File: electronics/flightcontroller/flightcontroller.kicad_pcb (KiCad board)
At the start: 2 copper layers, 30 x 50 mm, 81 parts, among them J1 BAT+, J10 USB, J11 Payload, J12 BAT-, J13 Conn_01x04, J2 ESC+, J3 ESC, J4 Servo3, J5 Servo2, J6 Servo1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

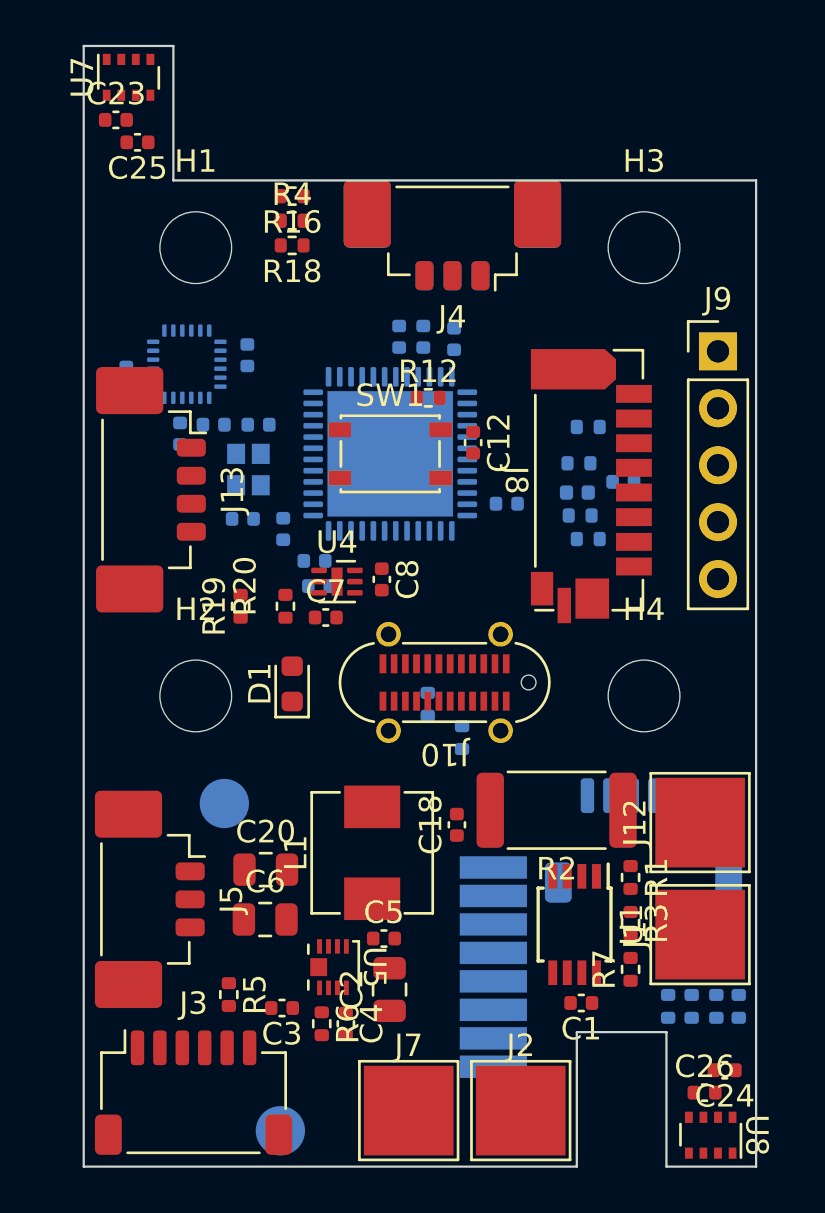
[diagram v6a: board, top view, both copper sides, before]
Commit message: electronics: Finished wiring of the flight controller PCB.
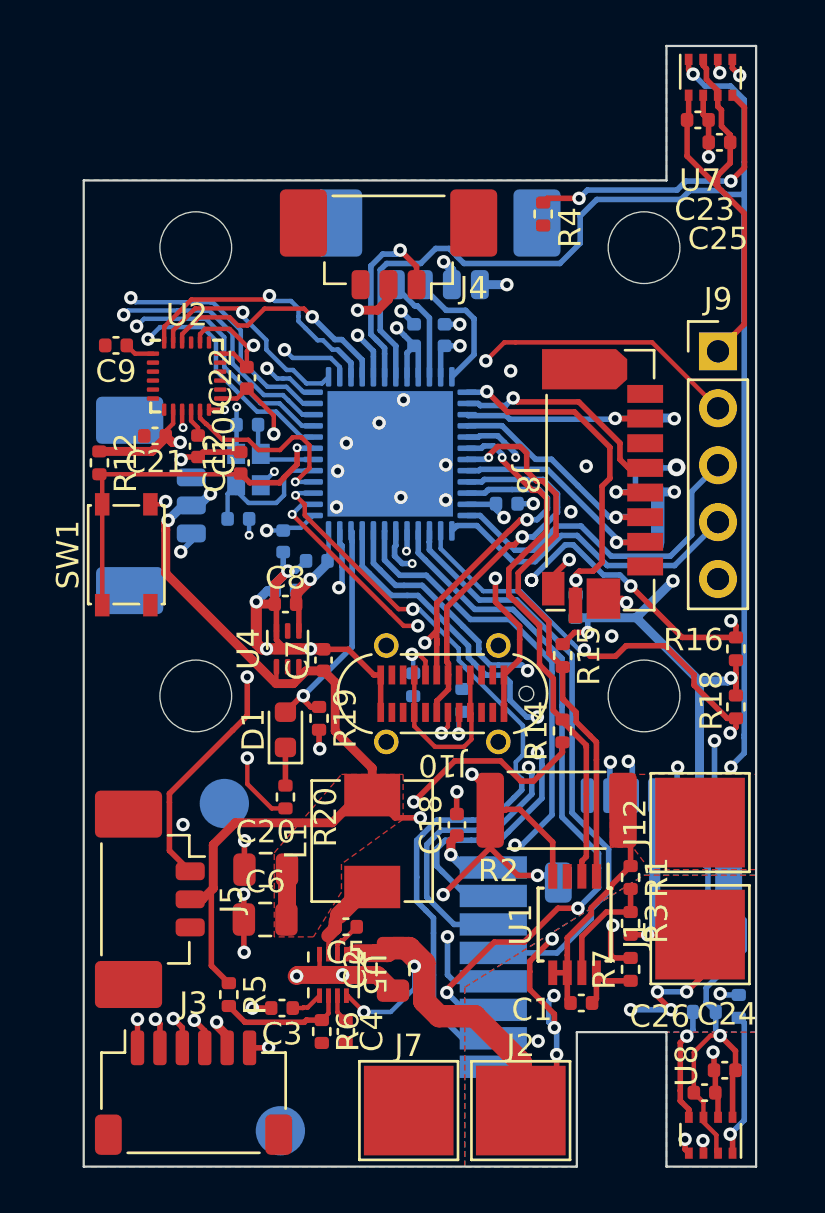
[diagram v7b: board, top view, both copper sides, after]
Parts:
- removed C13: 0.1uF, Capacitor_SMD:C_0402_1005Metric
- C10, C21, C22, C9, R14, R15, U2: moved to F.Cu
- C17: value 0.1uF -> 10uF
- J13: moved to B.Cu
- moved R18 28.6 mm to (214.1, 90.5), turned to -90 degrees
- moved R16 28.3 mm to (214.1, 87.9), turned to 90 degrees
- moved C23 26.0 mm to (212.4, 64.3)
- moved C25 26.0 mm to (213.4, 65.3)
- moved U7 26.0 mm to (213.0, 62.4)
- moved J6 17.3 mm to (188.6, 81.5), turned to 90 degrees
- moved R15 17.1 mm to (206.4, 88.2)
- moved J13 16.1 mm to (200.8, 70.4), turned to 0 degrees
- moved R12 15.0 mm to (185.7, 79.6), turned to -90 degrees
- moved R14 13.2 mm to (206.4, 91.6), turned to 90 degrees
- moved SW1 12.6 mm to (186.9, 83.7), turned to 90 degrees
- moved R4 11.2 mm to (205.5, 68.5), turned to -90 degrees
- moved C12 10.4 mm to (192.0, 79.6), turned to 90 degrees
- moved R20 8.51 mm to (194.0, 94.5), turned to -90 degrees
- moved R11 6.38 mm to (206.9, 86.0), turned to 90 degrees
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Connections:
- net Net-(C1-Pad2) renamed /Power Management/-BATT
- J11 pad MP: (no net) -> GND
- J13 pad MP: (no net) -> GND
- J3 pad MP: (no net) -> GND
- J4 pad MP: (no net) -> GND
- J5 pad MP: (no net) -> GND
- J6 pad MP: (no net) -> GND
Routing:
- net +3V3: track 0.00 -> 218.1 mm, vias 0 -> 17
- net GND: track 0.00 -> 119.4 mm, vias 0 -> 48
- net /MCU/PR_RST: track 0.00 -> 81.0 mm, vias 0 -> 3
- net +4V: track 0.00 -> 79.1 mm, vias 0 -> 6
- net /MCU/PR_SDA: track 0.00 -> 77.3 mm, vias 0 -> 7
- net /MCU/PR_SCL: track 0.00 -> 71.7 mm, vias 0 -> 4
- net +BATT: track 0.00 -> 46.6 mm, vias 0 -> 12
- net /MCU/PWM_M4: track 0.00 -> 45.9 mm, vias 0 -> 2
- net /MCU/PWM_M3: track 0.00 -> 45.7 mm, vias 0 -> 2
- net /MCU/PWM_M2: track 0.00 -> 44.6 mm, vias 0 -> 2
- net /MCU/PWM_M1: track 0.00 -> 44.0 mm, vias 0 -> 2
- net /MCU/~{RESET}: track 0.00 -> 38.8 mm, vias 0 -> 2
- net /MCU/RADIO_~{IRQ}: track 0.00 -> 35.6 mm, vias 0 -> 2
- net /MCU/RADIO_CE: track 0.00 -> 31.8 mm, vias 0 -> 3
- net /MCU/RADIO_MISO: track 0.00 -> 31.4 mm, vias 0 -> 2
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- added copper zone on F.Cu, net +4V
- added copper zone on B.Cu, net +BATT
- added copper zone on F.Cu, net +BATT
- added copper zone on In1.Cu, net +BATT
- added copper zone on F.Cu, net /Power Management/-BATT
- added copper zone on B.Cu, net GND
- added copper zone on F.Cu, net GND
- added copper zone on In1.Cu, net GND
- added copper zone on In2.Cu, net GND
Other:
- outline, holes or cut-outs redrawn
- copper layers 2 -> 4

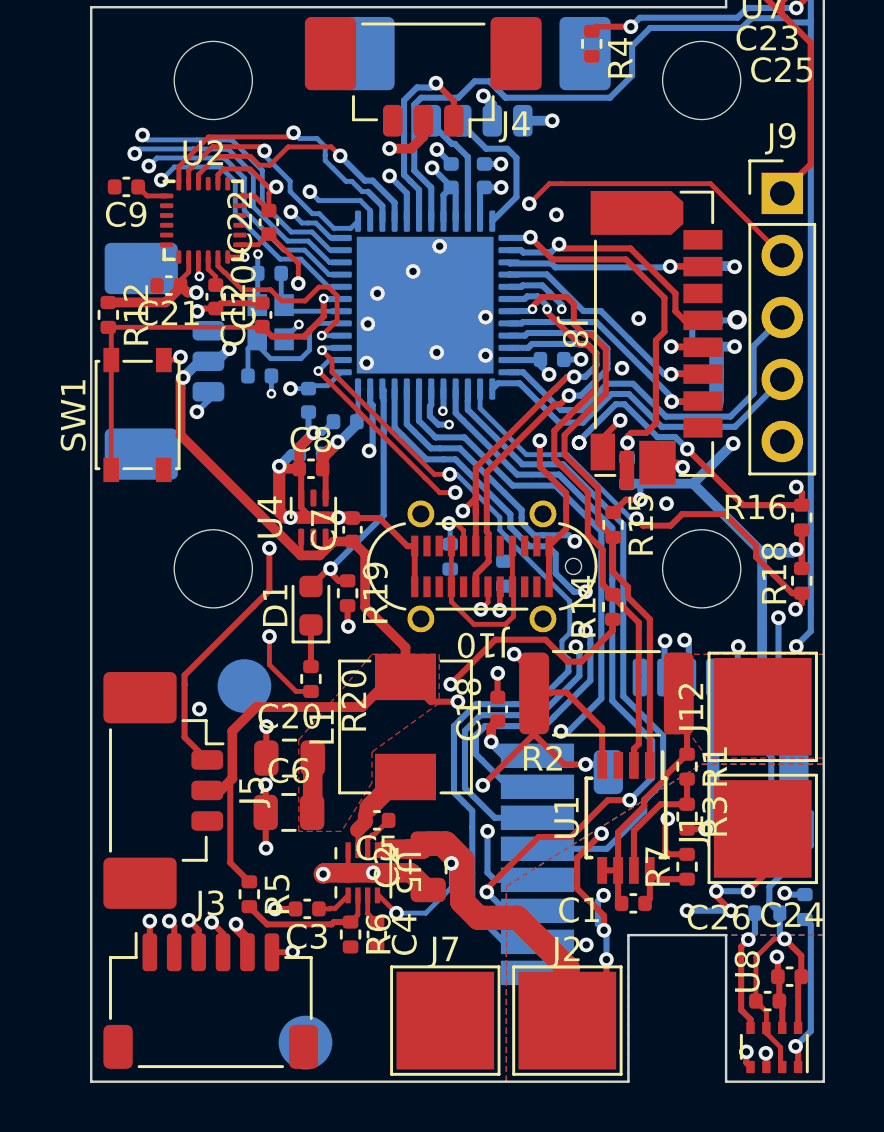
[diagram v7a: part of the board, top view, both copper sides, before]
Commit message: electronics: Fix most design rule checker errors.
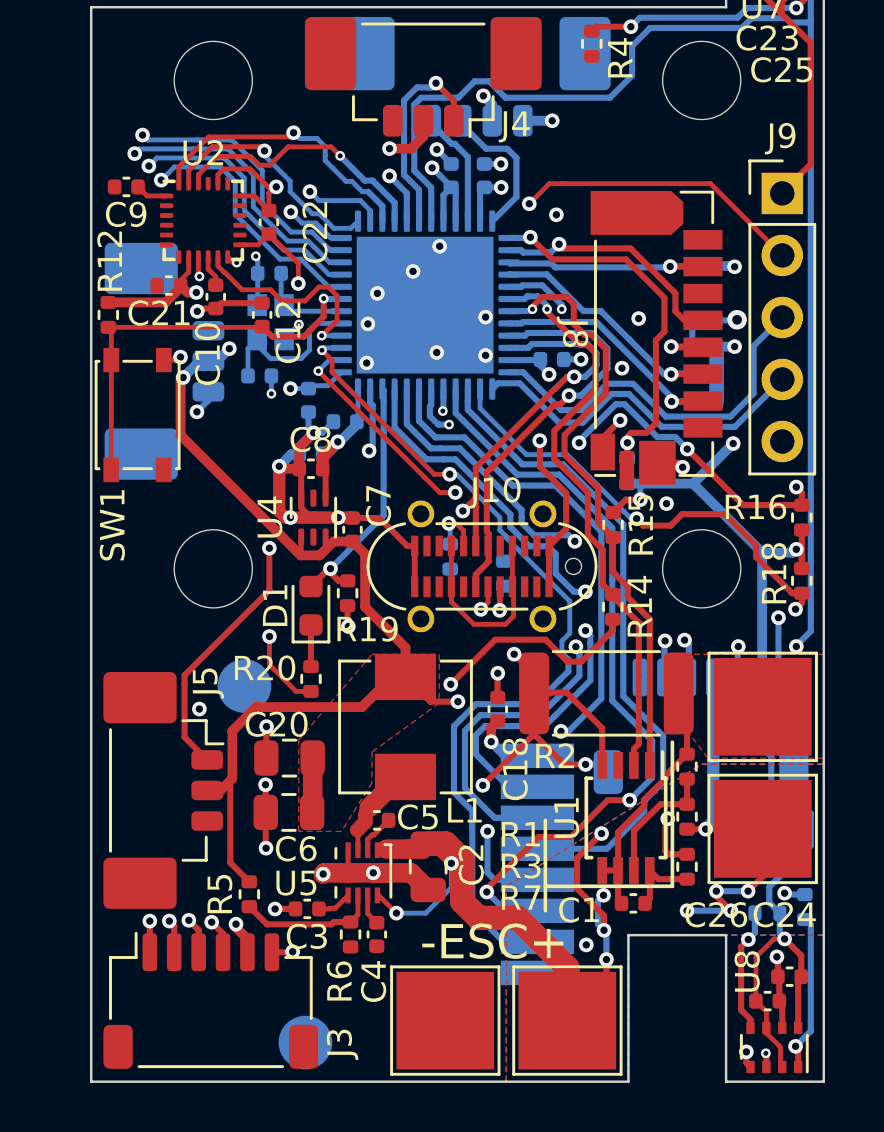
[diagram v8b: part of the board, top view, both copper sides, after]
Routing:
- net +3V3: track 218.1 -> 212.8 mm
- net GND: track 119.4 -> 117.7 mm
- net /MCU/PR_SDA: track 77.3 -> 77.2 mm, vias 7 -> 6
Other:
- board text added: "-ESC+"
